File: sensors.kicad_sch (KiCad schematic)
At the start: 12 parts, among them U4 IIM-42652, U5 BME280

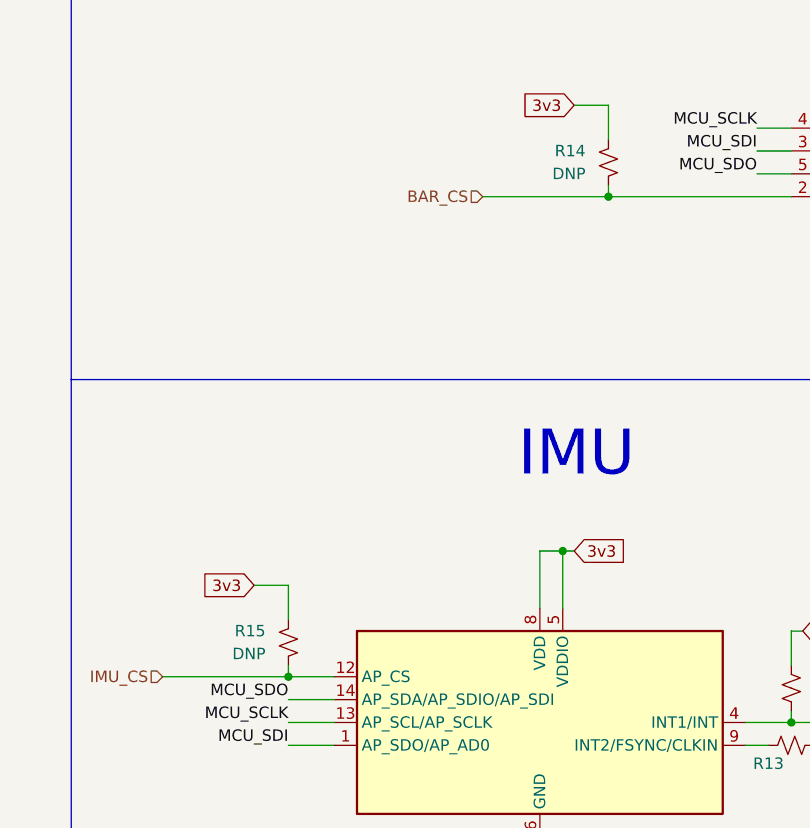
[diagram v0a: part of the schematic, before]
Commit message: Setup top sheet
Added TVS diodes, updated top sheet, misc label fixes
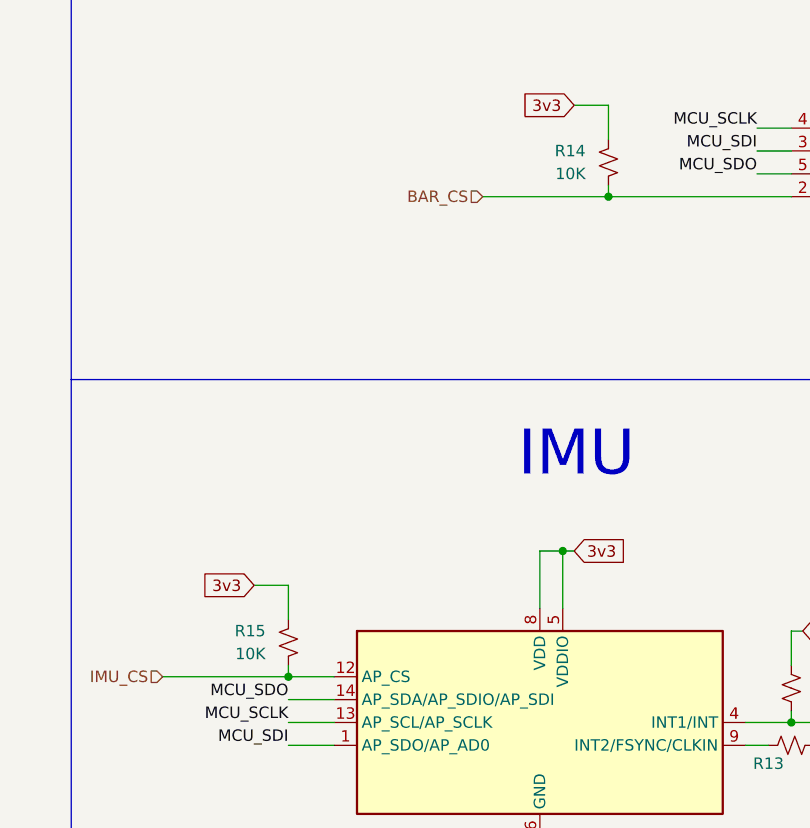
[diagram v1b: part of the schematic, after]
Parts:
- R14, R15: value DNP -> 10K
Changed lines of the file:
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@@
 			)
 		)
-		(property "Value" "DNP"
+		(property "Value" "10K"
 			(at 226.06 81.2799 0)
 			(effects
@@
 			)
 		)
-		(property "Value" "DNP"
+		(property "Value" "10K"
 			(at 190.5 134.6199 0)
 			(effects

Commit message: started layout
Preliminary footprint selection
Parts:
- C13, C14, C15, C16: footprint (none) -> Capacitor_SMD:C_0603_1608Metric_Pad1.08x0.95mm_HandSolder
- R13, R14, R15, R2: footprint (none) -> Resistor_SMD:R_0603_1608Metric
- TP5, TP6: footprint (none) -> TestPoint:TestPoint_Pad_1.0x1.0mm
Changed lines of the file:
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@@
 			)
 		)
-		(property "Footprint" ""
+		(property "Footprint" "Capacitor_SMD:C_0603_1608Metric_Pad1.08x0.95mm_HandSolder"
 			(at 54.61 180.34 0)
 			(effects
@@
 			)
 		)
-		(property "Footprint" ""
+		(property "Footprint" "Capacitor_SMD:C_0603_1608Metric_Pad1.08x0.95mm_HandSolder"
 			(at 33.02 180.34 0)
 			(effects
@@
 			)
 		)
-		(property "Footprint" ""
+		(property "Footprint" "TestPoint:TestPoint_Pad_1.0x1.0mm"
 			(at 264.16 140.97 0)
 			(effects
@@
 			)
 		)
-		(property "Footprint" ""
+		(property "Footprint" "Capacitor_SMD:C_0603_1608Metric_Pad1.08x0.95mm_HandSolder"
 			(at 22.86 180.34 0)
 			(effects
@@
 			)
 		)
-		(property "Footprint" ""
+		(property "Footprint" "TestPoint:TestPoint_Pad_1.0x1.0mm"
 			(at 254 144.78 0)
 			(effects
@@
 			)
 		)
-		(property "Footprint" ""
+		(property "Footprint" "Resistor_SMD:R_0603_1608Metric"
 			(at 248.92 144.78 0)
 			(effects
@@
 			)
 		)
-		(property "Footprint" ""
+		(property "Footprint" "Capacitor_SMD:C_0603_1608Metric_Pad1.08x0.95mm_HandSolder"
 			(at 44.45 180.34 0)
 			(effects
@@
 			)
 		)
-		(property "Footprint" ""
+		(property "Footprint" "Resistor_SMD:R_0603_1608Metric"
 			(at 248.92 138.43 0)
 			(effects
@@
 			)
 		)
-		(property "Footprint" ""
+		(property "Footprint" "Resistor_SMD:R_0603_1608Metric"
 			(at 228.6 80.01 0)
 			(effects
@@
 			)
 		)
-		(property "Footprint" ""
+		(property "Footprint" "Resistor_SMD:R_0603_1608Metric"
 			(at 193.04 133.35 0)
 			(effects

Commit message: footprint cleanup
switched to 0402 resistors, updated connectors, etc...
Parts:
- R13, R14, R15, R2: footprint Resistor_SMD:R_0603_1608Metric -> Resistor_SMD:R_0402_1005Metric
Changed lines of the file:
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@@
 			)
 		)
-		(property "Footprint" "Resistor_SMD:R_0603_1608Metric"
+		(property "Footprint" "Resistor_SMD:R_0402_1005Metric"
 			(at 248.92 144.78 0)
 			(effects
@@
 			)
 		)
-		(property "Footprint" "Resistor_SMD:R_0603_1608Metric"
+		(property "Footprint" "Resistor_SMD:R_0402_1005Metric"
 			(at 248.92 138.43 0)
 			(effects
@@
 			)
 		)
-		(property "Footprint" "Resistor_SMD:R_0603_1608Metric"
+		(property "Footprint" "Resistor_SMD:R_0402_1005Metric"
 			(at 228.6 80.01 0)
 			(effects
@@
 			)
 		)
-		(property "Footprint" "Resistor_SMD:R_0603_1608Metric"
+		(property "Footprint" "Resistor_SMD:R_0402_1005Metric"
 			(at 193.04 133.35 0)
 			(effects

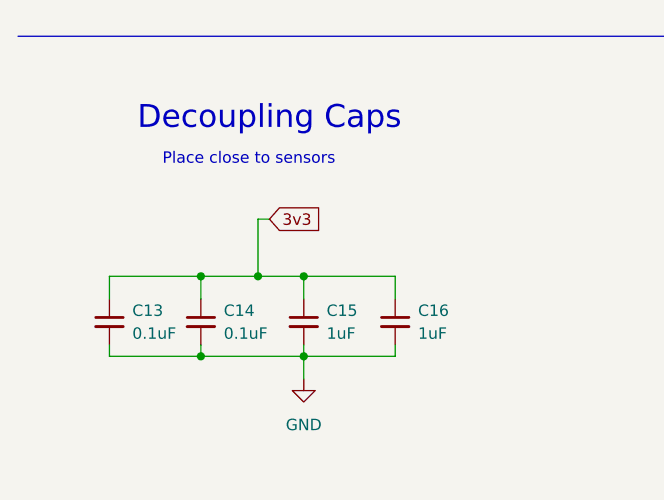
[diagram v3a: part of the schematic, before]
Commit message: Updates
Routing updates, placed expansion connector.
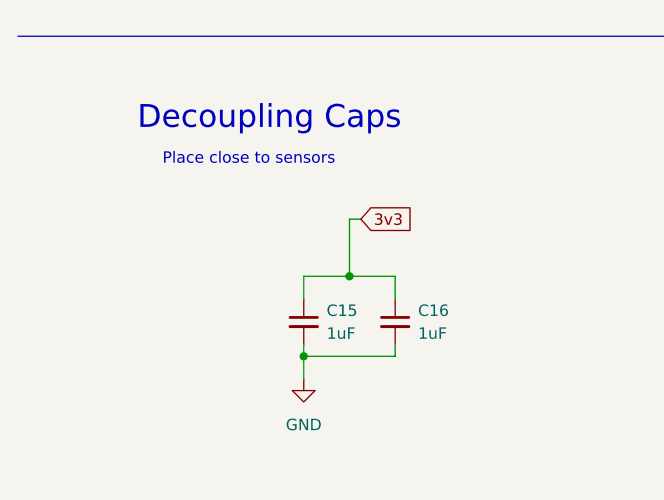
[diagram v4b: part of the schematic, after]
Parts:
- removed C13, C14: 0.1uF, Capacitor_SMD:C_0603_1608Metric_Pad1.08x0.95mm_HandSolder, symbol Device:C_Small
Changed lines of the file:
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@@
-	)
-	(junction
-		(at 33.02 184.15)
-		(diameter 0)
-		(color 0 0 0 0)
 	)
 	(junction
@@
 	)
 	(junction
-		(at 44.45 175.26)
-		(diameter 0)
-		(color 0 0 0 0)
-	)
-	(junction
 		(at 193.04 137.16)
-		(diameter 0)
-		(color 0 0 0 0)
-	)
-	(junction
-		(at 33.02 175.26)
 		(diameter 0)
 		(color 0 0 0 0)
@@
 	)
 	(junction
+		(at 49.53 175.26)
+		(diameter 0)
+		(color 0 0 0 0)
+	)
+	(junction
 		(at 259.08 144.78)
 		(diameter 0)
 		(color 0 0 0 0)
 	)
-	(junction
-		(at 39.37 175.26)
-		(diameter 0)
-		(color 0 0 0 0)
-	)
 	(wire
 		(pts
@@
 	(wire
 		(pts
-			(xy 54.61 175.26) (xy 44.45 175.26)
+			(xy 54.61 175.26) (xy 49.53 175.26)
 		)
 		(stroke
@@
 	(wire
 		(pts
-			(xy 44.45 184.15) (xy 33.02 184.15)
-		)
-		(stroke
-			(width 0)
-			(type default)
-		)
-	)
-	(wire
-		(pts
-			(xy 33.02 175.26) (xy 22.86 175.26)
-		)
-		(stroke
-			(width 0)
-			(type default)
-		)
-	)
-	(wire
-		(pts
-			(xy 22.86 175.26) (xy 22.86 177.8)
-		)
-		(stroke
-			(width 0)
-			(type default)
-		)
-	)
-	(wire
-		(pts
 			(xy 44.45 175.26) (xy 44.45 177.8)
 		)
@@
 	(wire
 		(pts
-			(xy 22.86 184.15) (xy 22.86 182.88)
-		)
-		(stroke
-			(width 0)
-			(type default)
-		)
-	)
-	(wire
-		(pts
-			(xy 39.37 168.91) (xy 40.64 168.91)
+			(xy 49.53 168.91) (xy 50.8 168.91)
 		)
 		(stroke
@@
 	(wire
 		(pts
-			(xy 44.45 175.26) (xy 39.37 175.26)
-		)
-		(stroke
-			(width 0)
-			(type default)
-		)
-	)
-	(wire
-		(pts
 			(xy 259.08 64.77) (xy 259.08 71.12)
 		)
@@
 	(wire
 		(pts
-			(xy 33.02 184.15) (xy 22.86 184.15)
-		)
-		(stroke
-			(width 0)
-			(type default)
-		)
-	)
-	(wire
-		(pts
 			(xy 248.92 135.89) (xy 248.92 132.08)
 		)
@@
 	(wire
 		(pts
-			(xy 39.37 175.26) (xy 39.37 168.91)
+			(xy 49.53 175.26) (xy 49.53 168.91)
 		)
 		(stroke
@@
 		)
 	)
-	(wire
-		(pts
-			(xy 33.02 184.15) (xy 33.02 182.88)
-		)
-		(stroke
-			(width 0)
-			(type default)
-		)
-	)
 	(polyline
 		(pts
@@
 	(wire
 		(pts
+			(xy 49.53 175.26) (xy 44.45 175.26)
+		)
+		(stroke
+			(width 0)
+			(type default)
+		)
+	)
+	(wire
+		(pts
 			(xy 259.08 140.97) (xy 259.08 142.24)
 		)
@@
 	(wire
 		(pts
-			(xy 39.37 175.26) (xy 33.02 175.26)
-		)
-		(stroke
-			(width 0)
-			(type default)
-		)
-	)
-	(wire
-		(pts
 			(xy 44.45 182.88) (xy 44.45 184.15)
 		)
@@
 		(pts
 			(xy 248.92 140.97) (xy 248.92 142.24)
-		)
-		(stroke
-			(width 0)
-			(type default)
-		)
-	)
-	(wire
-		(pts
-			(xy 33.02 175.26) (xy 33.02 177.8)
 		)
 		(stroke
@@
 	(global_label "3v3"
 		(shape input)
-		(at 40.64 168.91 0)
+		(at 50.8 168.91 0)
 		(fields_autoplaced yes)
 		(effects
@@
 		)
 		(property "Intersheetrefs" "${INTERSHEET_REFS}"
-			(at 46.4398 168.8306 0)
+			(at 56.5998 168.8306 0)
 			(effects
 				(font
@@
 	)
 	(symbol
-		(lib_id "Device:C_Small")
-		(at 33.02 180.34 0)
-		(unit 1)
-		(exclude_from_sim no)
-		(in_bom yes)
-		(on_board yes)
-		(dnp no)
-		(fields_autoplaced yes)
-		(property "Reference" "C14"
-			(at 35.56 179.0762 0)
-			(effects
-				(font
-					(size 1.27 1.27)
-				)
-				(justify left)
-			)
-		)
-		(property "Value" "0.1uF"
-			(at 35.56 181.6162 0)
-			(effects
-				(font
-					(size 1.27 1.27)
-				)
-				(justify left)
-			)
-		)
-		(property "Footprint" "Capacitor_SMD:C_0603_1608Metric_Pad1.08x0.95mm_HandSolder"
-			(at 33.02 180.34 0)
-			(effects
-				(font
-					(size 1.27 1.27)
-				)
-				(hide yes)
-			)
-		)
-		(property "Datasheet" "~"
-			(at 33.02 180.34 0)
-			(effects
-				(font
-					(size 1.27 1.27)
-				)
-				(hide yes)
-			)
-		)
-		(property "Description" "Unpolarized capacitor, small symbol"
-			(at 33.02 180.34 0)
-			(effects
-				(font
-					(size 1.27 1.27)
-				)
-				(hide yes)
-			)
-		)
-		(pin "2"
-		)
-		(pin "1"
-		)
-		(instances
-			(project "moon_child"
-				(path "/9fe08eae-9310-46cf-b272-eac4209a7b3e/b18c32a4-c727-4013-ad4f-289efcbafe2f"
-					(reference "C14")
-					(unit 1)
-				)
-			)
-		)
-	)
-	(symbol
 		(lib_id "Connector:TestPoint")
 		(at 259.08 140.97 0)
@@
 					(unit 1)
 				)
-			)
-		)
-	)
-	(symbol
-		(lib_id "Device:C_Small")
-		(at 22.86 180.34 0)
-		(unit 1)
-		(exclude_from_sim no)
-		(in_bom yes)
-		(on_board yes)
-		(dnp no)
-		(fields_autoplaced yes)
-		(property "Reference" "C13"
-			(at 25.4 179.0762 0)
-			(effects
-				(font
-					(size 1.27 1.27)
-				)
-				(justify left)
-			)
-		)
-		(property "Value" "0.1uF"
-			(at 25.4 181.6162 0)
-			(effects
-				(font
-					(size 1.27 1.27)
-				)
-				(justify left)
-			)
-		)
-		(property "Footprint" "Capacitor_SMD:C_0603_1608Metric_Pad1.08x0.95mm_HandSolder"
-			(at 22.86 180.34 0)
-			(effects
-				(font
-					(size 1.27 1.27)
-				)
-				(hide yes)
-			)
-		)
-		(property "Datasheet" "~"
-			(at 22.86 180.34 0)
-			(effects
-				(font
-					(size 1.27 1.27)
-				)
-				(hide yes)
-			)
-		)
-		(property "Description" "Unpolarized capacitor, small symbol"
-			(at 22.86 180.34 0)
-			(effects
-				(font
-					(size 1.27 1.27)
-				)
-				(hide yes)
-			)
-		)
-		(pin "2"
-		)
-		(pin "1"
-		)
-		(instances
-			(project "moon_child"
-				(path "/9fe08eae-9310-46cf-b272-eac4209a7b3e/b18c32a4-c727-4013-ad4f-289efcbafe2f"
-					(reference "C13")
-					(unit 1)
-				)

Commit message: Layout updates
testpoints, usb power, etc.
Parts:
- TP5, TP6: footprint TestPoint:TestPoint_Pad_1.0x1.0mm -> TestPoint:TestPoint_Pad_D1.0mm
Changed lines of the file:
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@@
 			)
 		)
-		(property "Footprint" "TestPoint:TestPoint_Pad_1.0x1.0mm"
+		(property "Footprint" "TestPoint:TestPoint_Pad_D1.0mm"
 			(at 264.16 140.97 0)
 			(effects
@@
 			)
 		)
-		(property "Footprint" "TestPoint:TestPoint_Pad_1.0x1.0mm"
+		(property "Footprint" "TestPoint:TestPoint_Pad_D1.0mm"
 			(at 254 144.78 0)
 			(effects

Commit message: Bom updates
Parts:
- C15, C16: MPN (none) -> CL10B105KP8NNNC; Package (none) -> 0603
- R13: MPN (none) -> RC0402FR-070RL; Package (none) -> 0402
- R14, R15, R2: MPN (none) -> RC0402JR-0710KL; Package (none) -> 0402
- TP5, TP6: now not fitted
- U4: MPN (none) -> IIM-42652; Package (none) -> 14-VFLGA
- U5: MPN (none) -> BME280; Package (none) -> 8-VFLGA
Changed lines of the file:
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@@
+			)
+		)
+		(property "MPN" "CL10B105KP8NNNC"
+			(at 54.61 180.34 0)
+			(effects
+				(font
+					(size 1.27 1.27)
+				)
+				(hide yes)
+			)
+		)
+		(property "Package" "0603"
+			(at 54.61 180.34 0)
+			(effects
+				(font
+					(size 1.27 1.27)
+				)
+				(hide yes)
 			)
 		)
@@
 		(in_bom yes)
 		(on_board yes)
-		(dnp no)
+		(dnp yes)
 		(fields_autoplaced yes)
 		(property "Reference" "TP5"
@@
 		(in_bom yes)
 		(on_board yes)
-		(dnp no)
+		(dnp yes)
 		(fields_autoplaced yes)
 		(property "Reference" "TP6"
@@
 		)
 		(property "Description" "Resistor, small US symbol"
+			(at 248.92 144.78 0)
+			(effects
+				(font
+					(size 1.27 1.27)
+				)
+				(hide yes)
+			)
+		)
+		(property "Package" "0402"
+			(at 248.92 144.78 0)
+			(effects
+				(font
+					(size 1.27 1.27)
+				)
+				(hide yes)
+			)
+		)
+		(property "MPN" "RC0402FR-070RL"
 			(at 248.92 144.78 0)
 			(effects
@@
 			)
 		)
+		(property "MPN" "CL10B105KP8NNNC"
+			(at 44.45 180.34 0)
+			(effects
+				(font
+					(size 1.27 1.27)
+				)
+				(hide yes)
+			)
+		)
+		(property "Package" "0603"
+			(at 44.45 180.34 0)
+			(effects
+				(font
+					(size 1.27 1.27)
+				)
+				(hide yes)
+			)
+		)
 		(pin "2"
 		)
@@
 			)
 		)
+		(property "MPN" "IIM-42652"
+			(at 220.98 142.24 0)
+			(effects
+				(font
+					(size 1.27 1.27)
+				)
+				(hide yes)
+			)
+		)
+		(property "Package" "14-VFLGA"
+			(at 220.98 142.24 0)
+			(effects
+				(font
+					(size 1.27 1.27)
+				)
+				(hide yes)
+			)
+		)
 		(pin "12"
 		)
@@
 			)
 		)
+		(property "Package" "0402"
+			(at 248.92 138.43 0)
+			(effects
+				(font
+					(size 1.27 1.27)
+				)
+				(hide yes)
+			)
+		)
+		(property "MPN" "RC0402JR-0710KL"
+			(at 248.92 138.43 0)
+			(effects
+				(font
+					(size 1.27 1.27)
+				)
+				(hide yes)
+			)
+		)
 		(pin "2"
 		)
@@
 			)
 		)
+		(property "MPN" "BME280"
+			(at 259.08 81.28 0)
+			(effects
+				(font
+					(size 1.27 1.27)
+				)
+				(hide yes)
+			)
+		)
+		(property "Package" "8-VFLGA"
+			(at 259.08 81.28 0)
+			(effects
+				(font
+					(size 1.27 1.27)
+				)
+				(hide yes)
+			)
+		)
 		(pin "4"
 		)
@@
 			)
 		)
+		(property "Package" "0402"
+			(at 228.6 80.01 0)
+			(effects
+				(font
+					(size 1.27 1.27)
+				)
+				(hide yes)
+			)
+		)
+		(property "MPN" "RC0402JR-0710KL"
+			(at 228.6 80.01 0)
+			(effects
+				(font
+					(size 1.27 1.27)
+				)
+				(hide yes)
+			)
+		)
 		(pin "2"
 		)
@@
 			(at 193.04 133.35 0)
 			(effects
+				(font
+					(size 1.27 1.27)
+				)
+				(hide yes)
+			)
+		)
+		(property "Package" "0402"
+			(at 193.04 133.35 0)
+			(effects
+				(font
+					(size 1.27 1.27)
+				)
+				(hide yes)
+			)
+		)
+		(property "MPN" "RC0402JR-0710KL"
+			(at 193.04 133.35 0)
+			(effects
